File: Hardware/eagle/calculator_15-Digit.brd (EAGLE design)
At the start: 154.9 x 53.3 mm, 145 parts, among them M1 IRLML6402, M10 IRLML6402, M11 IRLML6402, M12 IRLML6402, M2 IRLML6402, M3 IRLML6402, M4 IRLML6402, M5 IRLML6402, M6 IRLML6402, M7 IRLML6402, M8 IRLML6402, M9 IRLML6402, U1 74HC4051_MUX, U2 TC1262-3.3VDB, U3 ATMEGA1284P-PU, U5 CON, X1 MICROMATCH-12, X3 MICROMATCH-12, Y2 12MHz

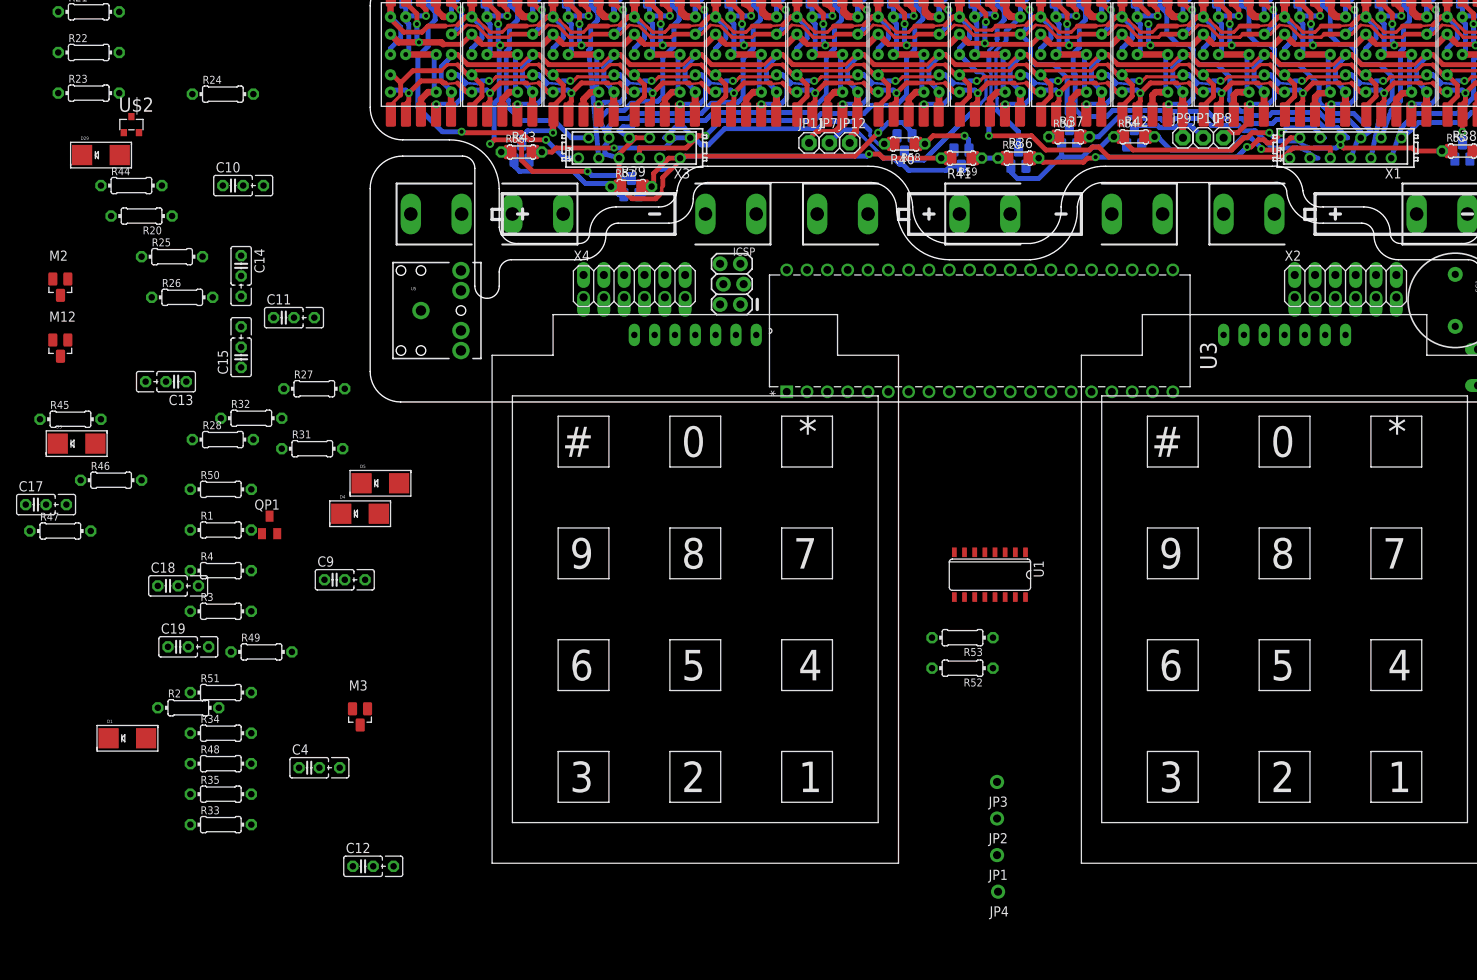
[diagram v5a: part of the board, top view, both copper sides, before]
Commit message: new Switch Layout - with Kipptaster
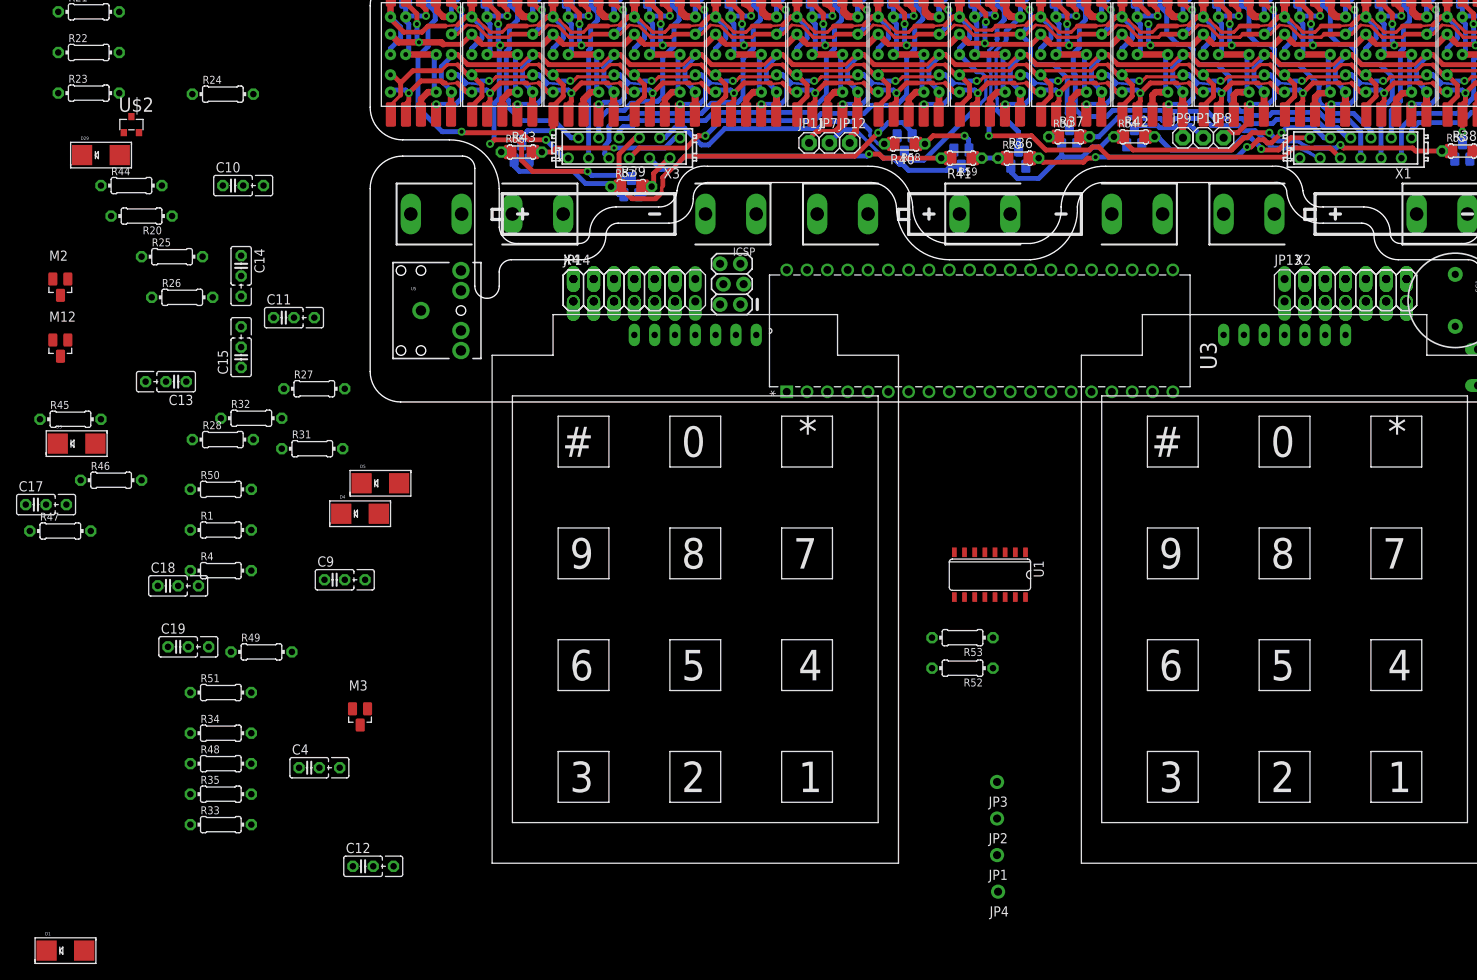
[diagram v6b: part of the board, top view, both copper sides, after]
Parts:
- removed QP1: BC327-25, sym:SOT23
- removed R2, R3: 6k8, rcl:0204/7
- added JP13, JP14: PINHD-2X7, pinhead:ZX07
- R50: value 8k2 -> 6k8
- moved D1 27.7 mm to (-38.1, -68.6)
- moved X4 1.37 mm to (31.8, 14.0)
- moved X2 1.37 mm to (123.2, 14.0)
- moved X3 1.27 mm to (31.8, 31.8)
- moved X1 1.27 mm to (123.2, 31.8)
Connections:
- removed net N$10: QP1.3, R1.1
- removed net N$13: QP1.2, R2.1, R50.2
- net /RESET: no longer D1.A
- net 3V5: now also R1.1; no longer D1.C, QP1.1, R2.2, R3.2
- net AREF: no longer R3.1
- net CA_PWM: now also JP13.1, JP13.2, JP14.13, JP14.14, JP14.8
- net D10: now also JP13.9
- net D11: now also JP13.10
- net D12: now also JP14.1
- net D13: now also JP14.2
- net D19: now also JP14.7
- net D20: now also JP14.6
- net D21: now also JP14.5
- net D22: now also JP14.4
- net D23: now also JP14.3
- net D5: now also JP13.8
- net D6: now also JP13.7
- net D7: now also JP6.2
- net GND: now also D1.A
- net IO_A: now also JP13.6
- net IO_A__: now also JP13.11
- net IO_B: now also JP13.5
- net IO_B__: now also JP13.12
- net IO_C: now also JP13.4
- net IO_C__: now also JP13.13
- net IO_D: now also JP13.3
- net IO_DP: now also JP14.9
- net IO_D__: now also JP13.14
- net IO_E: now also JP14.12
- net IO_F: now also JP14.11
- net IO_G: now also JP14.10
- net N$12: now also D1.C
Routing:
- net IO-E: track 22.7 -> 21.5 mm
- net D0_A: track 37.7 -> 36.4 mm
- net IO-F: track 9.14 -> 7.87 mm
- net IO-C: track 24.1 -> 25.4 mm
- net D1_A: track 26.4 -> 25.2 mm
- net CA_LED: track 164.4 -> 163.1 mm
- net D4_A: track 37.5 -> 36.3 mm
- net IO-B: track 36.2 -> 35.4 mm
- net D5_A: track 42.6 -> 42.0 mm
- net D10_A: track 28.9 -> 28.3 mm
- net D14_A: track 34.9 -> 34.3 mm
- net IO-DP: track 40.6 -> 41.2 mm
- net D7_A: track 64.7 -> 65.3 mm
- net D6_A: track 50.8 -> 51.3 mm
- net D8_A: track 52.6 -> 52.1 mm

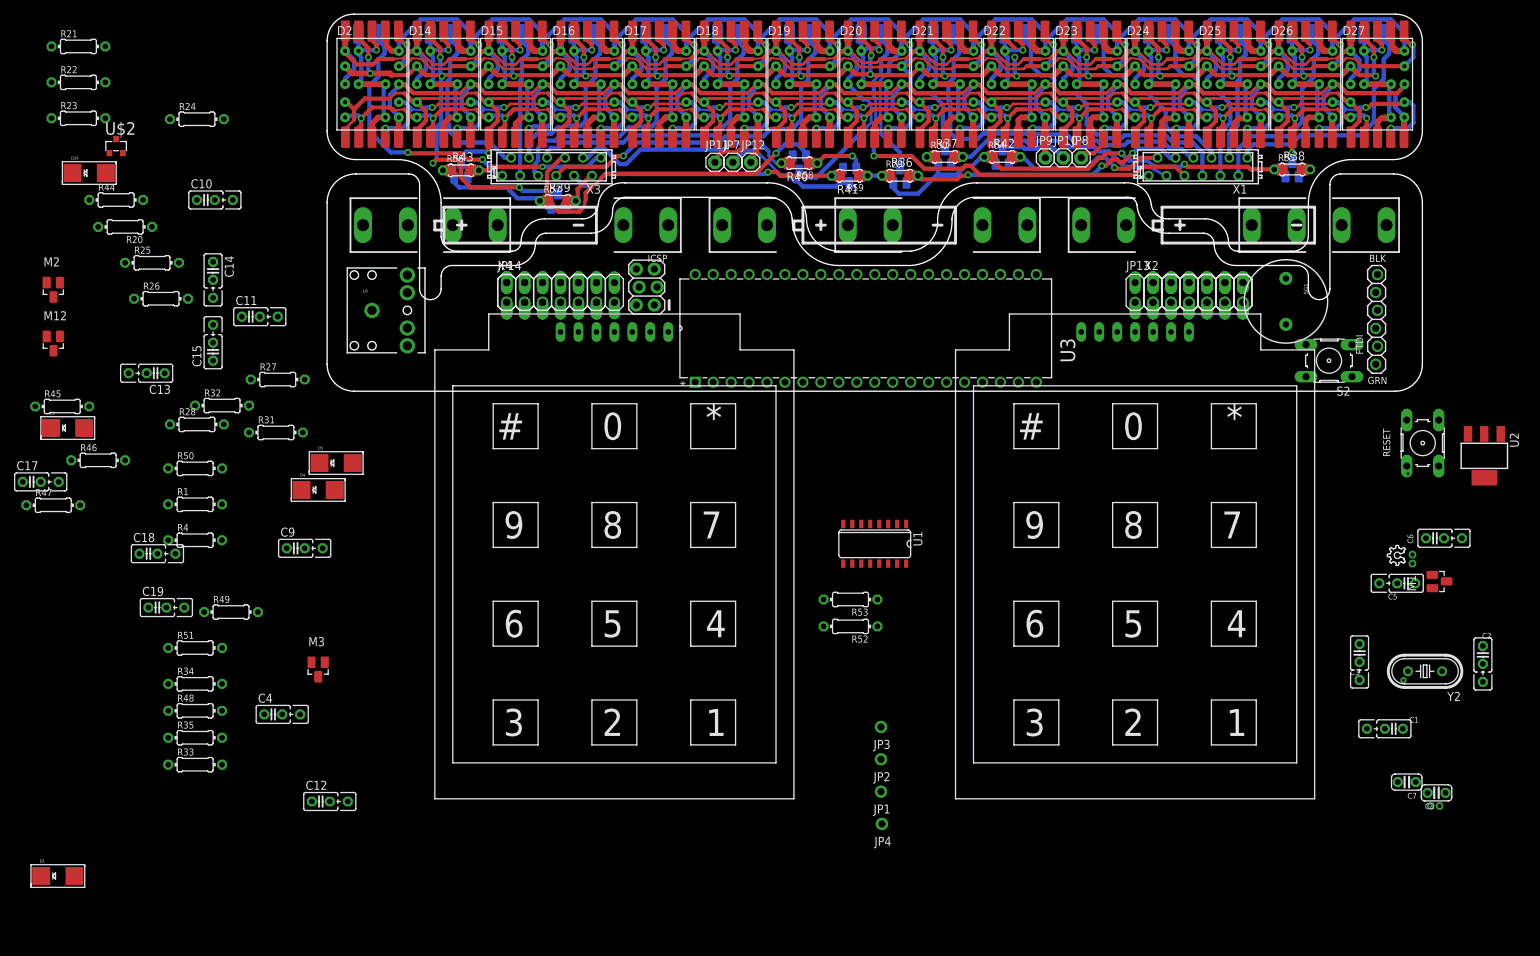
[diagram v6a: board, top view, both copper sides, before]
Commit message: MR(); MS(); M+=(); Display Status
Display whe to or more switch pressed.
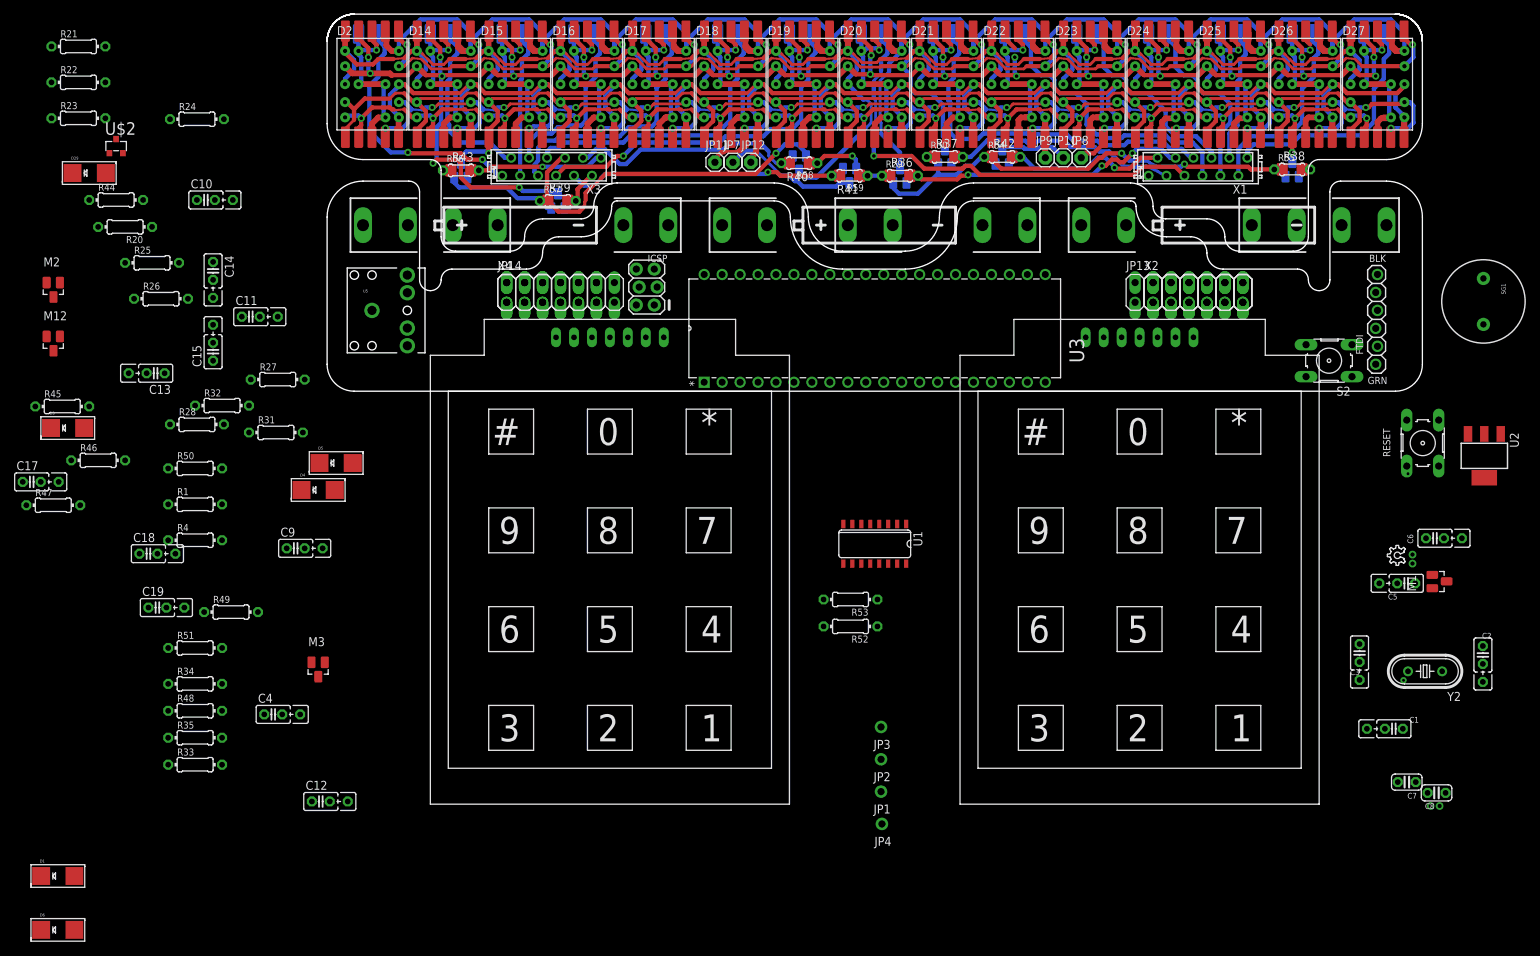
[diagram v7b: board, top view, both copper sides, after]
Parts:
- added D6: SD103CW, BaseApp:SMADIODE
- moved SG1 27.9 mm to (163.6, 12.7)
- moved U3 1.27 mm to (101.6, 16.5)
- moved KP2 0.99 mm to (114.9, 7.62)
- moved KP1 0.99 mm to (40.0, 7.62)
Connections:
- net /RESET: now also D6.A
- net 3V5: now also D6.C
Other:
- outline, holes or cut-outs redrawn

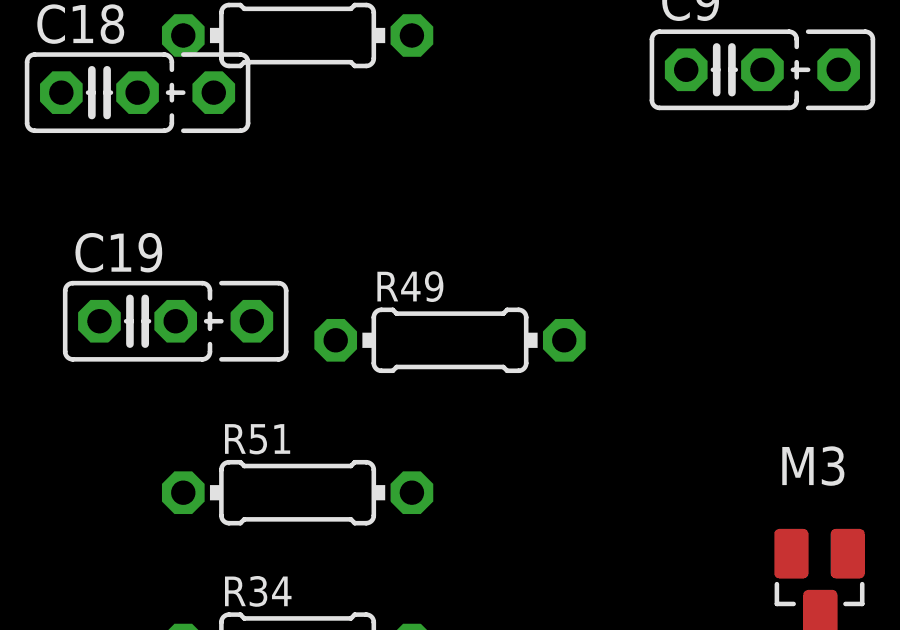
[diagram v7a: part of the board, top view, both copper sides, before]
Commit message: RingBufCPP added
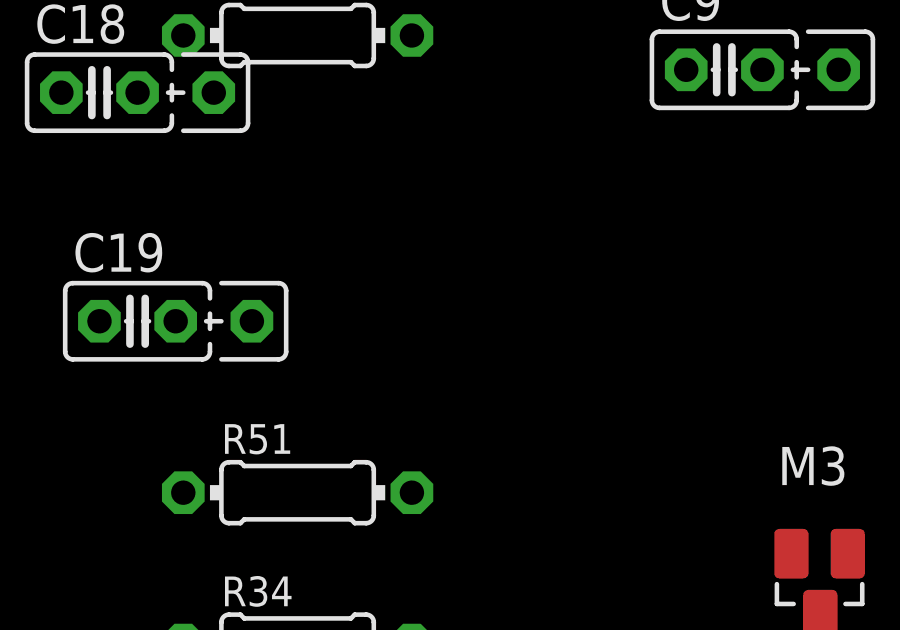
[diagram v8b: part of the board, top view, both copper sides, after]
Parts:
- removed R49: 100k, rcl:0204/7
- M10, M11, M3, M4, M5, M6, M7, M8, M9: value IRLML6402 -> IRLML6401
- R1: value 27k -> 68k
- R51: value 1k -> 3k3
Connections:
- net /RESET: no longer R49.2
- net N$12: no longer R49.1
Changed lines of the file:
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@@
 <layer number="50" name="dxf" color="7" fill="1" visible="no" active="yes"/>
 <layer number="51" name="tDocu" color="6" fill="1" visible="yes" active="yes"/>
-<layer number="52" name="bDocu" color="7" fill="1" visible="no" active="yes"/>
+<layer number="52" name="bDocu" color="7" fill="1" visible="yes" active="yes"/>
 <layer number="53" name="tGND_GNDA" color="7" fill="9" visible="no" active="no"/>
 <layer number="54" name="bGND_GNDA" color="1" fill="9" visible="no" active="no"/>
@@
 <element name="R32" library="rcl" package="0204/7" value="100" x="-14.859" y="-2.032"/>
 <element name="U1" library="SparkFun-AnalogIC" package="SO16" value="74HC4051_MUX" x="77.47" y="-21.59" rot="R180"/>
-<element name="M3" library="IRLML6402" package="SOT-23" value="IRLML6402" x="-1.27" y="-39.37"/>
-<element name="M4" library="IRLML6402" package="SOT-23" value="IRLML6402" x="81.026" y="30.48" rot="MR180"/>
-<element name="M5" library="IRLML6402" package="SOT-23" value="IRLML6402" x="87.376" y="33.147" rot="MR180"/>
-<element name="M6" library="IRLML6402" package="SOT-23" value="IRLML6402" x="95.504" y="33.147" rot="MR180"/>
-<element name="M7" library="IRLML6402" package="SOT-23" value="IRLML6402" x="136.525" y="31.369" rot="MR180"/>
-<element name="M8" library="IRLML6402" package="SOT-23" value="IRLML6402" x="18.923" y="31.242" rot="MR180"/>
-<element name="M9" library="IRLML6402" package="SOT-23" value="IRLML6402" x="32.639" y="26.924" rot="MR180"/>
-<element name="M10" library="IRLML6402" package="SOT-23" value="IRLML6402" x="66.802" y="32.258" rot="MR0"/>
-<element name="M11" library="IRLML6402" package="SOT-23" value="IRLML6402" x="73.914" y="30.48" rot="MR0"/>
+<element name="M3" library="IRLML6402" package="SOT-23" value="IRLML6401" x="-1.27" y="-39.37"/>
+<element name="M4" library="IRLML6402" package="SOT-23" value="IRLML6401" x="81.026" y="30.48" rot="MR180"/>
+<element name="M5" library="IRLML6402" package="SOT-23" value="IRLML6401" x="87.376" y="33.147" rot="MR180"/>
+<element name="M6" library="IRLML6402" package="SOT-23" value="IRLML6401" x="95.504" y="33.147" rot="MR180"/>
+<element name="M7" library="IRLML6402" package="SOT-23" value="IRLML6401" x="136.525" y="31.369" rot="MR180"/>
+<element name="M8" library="IRLML6402" package="SOT-23" value="IRLML6401" x="18.923" y="31.242" rot="MR180"/>
+<element name="M9" library="IRLML6402" package="SOT-23" value="IRLML6401" x="32.639" y="26.924" rot="MR180"/>
+<element name="M10" library="IRLML6402" package="SOT-23" value="IRLML6401" x="66.802" y="32.258" rot="MR0"/>
+<element name="M11" library="IRLML6402" package="SOT-23" value="IRLML6401" x="73.914" y="30.48" rot="MR0"/>
 <element name="D29" library="BaseApp" package="SMADIODE" value="SD103CW" x="-33.655" y="30.861"/>
 <element name="U$2" library="transistor-power" package="MICRO3" value="IRLML2502" x="-29.845" y="34.671"/>
@@
 </element>
 <element name="R50" library="rcl" package="0204/7" value="6k8" x="-18.669" y="-10.922"/>
-<element name="R1" library="rcl" package="0204/7" value="27k" x="-18.669" y="-16.002"/>
+<element name="R1" library="rcl" package="0204/7" value="68k" x="-18.669" y="-16.002"/>
 <element name="R4" library="rcl" package="0204/7" value="100" x="-18.669" y="-21.082"/>
-<element name="R49" library="rcl" package="0204/7" value="100k" x="-13.589" y="-31.242"/>
-<element name="R51" library="rcl" package="0204/7" value="1k" x="-18.669" y="-36.322"/>
+<element name="R51" library="rcl" package="0204/7" value="3k3" x="-18.669" y="-36.322"/>
 <element name="R34" library="rcl" package="0204/7" value="6k8" x="-18.669" y="-41.402"/>
 <element name="R48" library="rcl" package="0204/7" value="1k" x="-18.669" y="-45.212"/>
@@
 <contactref element="U3" pad="9"/>
 <contactref element="R1" pad="2"/>
-<contactref element="R49" pad="2"/>
 <contactref element="D6" pad="A"/>
 <wire x1="157.2514" y1="-10.5918" x2="157.2514" y2="-4.0894" width="0" layer="19" extent="1-1"/>
@@
 <wire x1="-14.859" y1="-16.002" x2="46.2788" y2="17.272" width="0" layer="19" extent="1-1"/>
 <wire x1="-26.543" y1="-22.987" x2="-14.859" y2="-16.002" width="0" layer="19" extent="1-1"/>
-<wire x1="-9.779" y1="-31.242" x2="-14.859" y2="-16.002" width="0" layer="19" extent="1-1"/>
-<wire x1="-35.7505" y1="-76.2" x2="-9.779" y2="-31.242" width="0" layer="19" extent="1-1"/>
+<wire x1="-35.7505" y1="-76.2" x2="-26.543" y2="-22.987" width="0" layer="19" extent="1-1"/>
 </signal>
 <signal name="D13">
@@
 <contactref element="C18" pad="2"/>
 <contactref element="JP6" pad="6"/>
-<contactref element="R49" pad="1"/>
 <contactref element="R51" pad="2"/>
 <contactref element="D1" pad="C"/>
 <wire x1="-14.859" y1="-36.322" x2="148.336" y2="3.81" width="0" layer="19" extent="1-1"/>
-<wire x1="-17.399" y1="-31.242" x2="-14.859" y2="-36.322" width="0" layer="19" extent="1-1"/>
-<wire x1="-24.003" y1="-22.987" x2="-17.399" y2="-31.242" width="0" layer="19" extent="1-1"/>
+<wire x1="-24.003" y1="-22.987" x2="-14.859" y2="-36.322" width="0" layer="19" extent="1-1"/>
 <wire x1="-40.4495" y1="-68.58" x2="-14.859" y2="-36.322" width="0" layer="19" extent="1-1"/>
 </signal>
